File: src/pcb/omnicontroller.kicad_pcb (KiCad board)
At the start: 2 copper layers, 124.5 x 68.6 mm, 52 parts, among them J1 G-Switch GT-USB-7010ASV, J2 USB_A, U1 RP2040, U2 NCP1117ST33T3G, U3 W25Q128JVSIM, X1 SW_Omron_B3FS-1000P, Y1 ABM8-272-T3, Y2 SW_Omron_B3FS-1000P

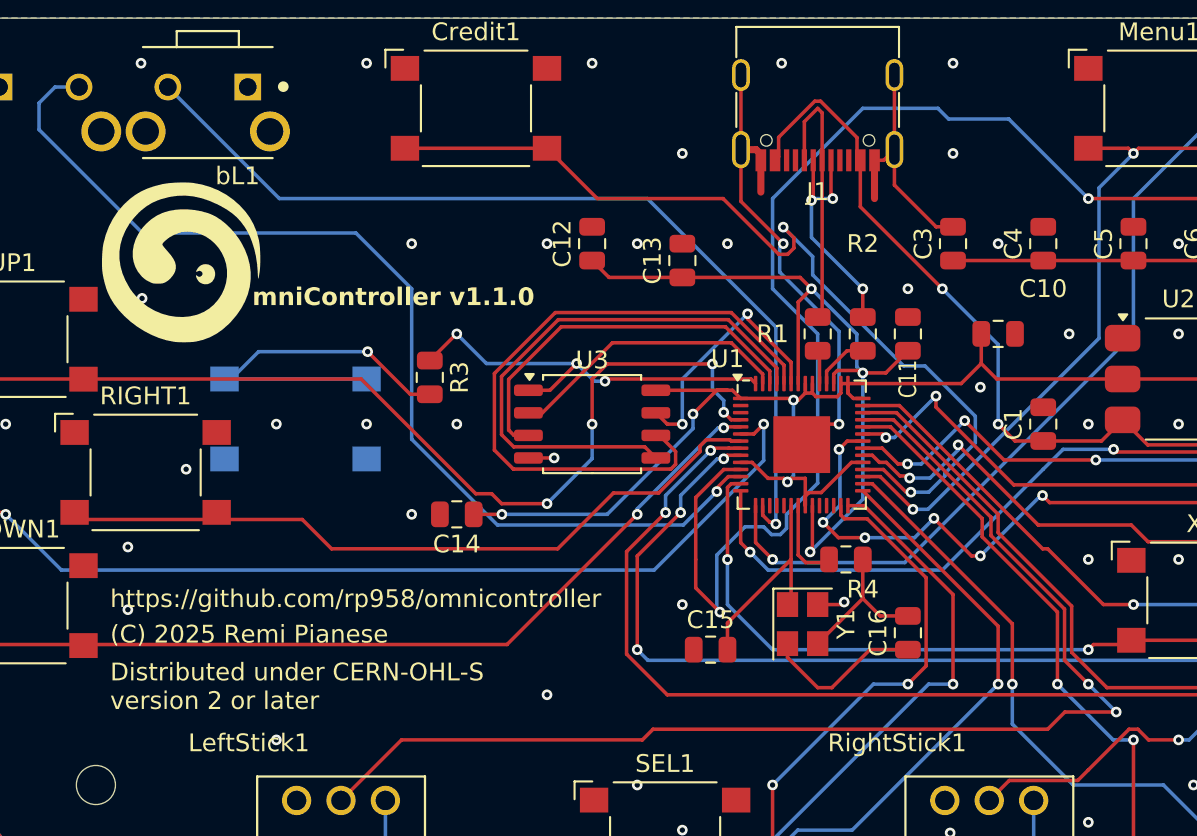
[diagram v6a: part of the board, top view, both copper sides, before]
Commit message: add pinheader with all unused GPIO
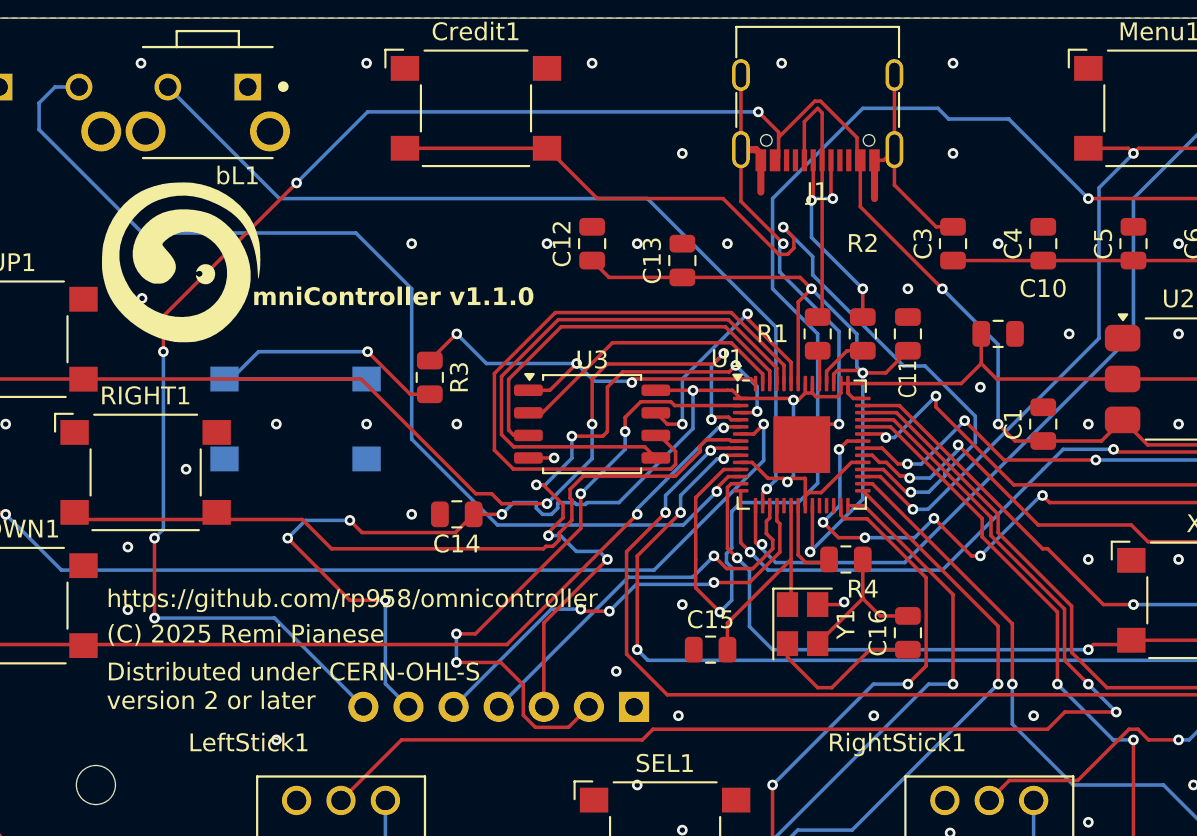
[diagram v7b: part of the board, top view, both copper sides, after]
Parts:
- added J3: Conn_01x07_Pin, Connector_PinHeader_2.54mm:PinHeader_1x07_P2.54mm_Horizontal, B.Cu at (106.5, 84.5)
- START1: value SW_Omron_B3FS-1000P -> SW_Omron_B3FS-1000
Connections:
- U1 pad 17: unconnected-(U1-GPIO14-Pad17) -> GP14
- U1 pad 18: unconnected-(U1-GPIO15-Pad18) -> GP15
- U1 pad 2: unconnected-(U1-GPIO0-Pad2) -> GP00
- U1 pad 3: unconnected-(U1-GPIO1-Pad3) -> GP01
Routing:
- net VBUS: track 83.7 -> 155.0 mm, vias 3 -> 8
- net GP01: track 0.00 -> 38.0 mm, vias 0 -> 6
- net GP00: track 0.00 -> 35.8 mm, vias 0 -> 4
- net +3V3: track 257.1 -> 282.0 mm, vias 7 -> 10
- net GP15: track 0.00 -> 24.8 mm, vias 0 -> 3
- net GP14: track 0.00 -> 22.4 mm, vias 0 -> 1
- net GP02: track 56.3 -> 58.9 mm
- net GP13: track 52.3 -> 50.2 mm
- net GP05: track 41.1 -> 42.5 mm
- net GND: vias 90 -> 93

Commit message: Add 3d models to pcb
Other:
- board text added: "+3.3V"
- board text added: "+5V"
- board text added: "GND"
- board text added: "GP00"
- board text added: "GP01"
- board text added: "GP14"
- board text added: "GP15"
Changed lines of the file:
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@@
 		)
 		(embedded_fonts no)
-		(model "${KICAD6_3DMODEL_DIR}/Button_Switch_SMD.3dshapes/SW_SPST_Omron_B3FS-100xP.wrl"
+		(model "${KIPRJMOD}/libs/Buttons.pretty/B3FS-1000--3DModel-STEP-273799.STEP"
 			(offset
 				(xyz 0 0 0)
@@
 			)
 			(rotate
-				(xyz 0 0 0)
+				(xyz -90 -0 -0)
 			)
 		)
@@
 		)
 		(embedded_fonts no)
-		(model "${KICAD6_3DMODEL_DIR}/Button_Switch_SMD.3dshapes/SW_SPST_Omron_B3FS-100xP.wrl"
+		(model "${KIPRJMOD}/libs/Buttons.pretty/B3FS-1000--3DModel-STEP-273799.STEP"
 			(offset
 				(xyz 0 0 0)
@@
 			)
 			(rotate
-				(xyz 0 0 0)
+				(xyz -90 -0 -0)
 			)
 		)
@@
 		)
 		(embedded_fonts no)
-		(model "${KICAD6_3DMODEL_DIR}/Button_Switch_SMD.3dshapes/SW_SPST_Omron_B3FS-100xP.wrl"
+		(model "${KIPRJMOD}/libs/Buttons.pretty/B3FS-1000--3DModel-STEP-273799.STEP"
 			(offset
 				(xyz 0 0 0)
@@
 			)
 			(rotate
-				(xyz 0 0 0)
+				(xyz -90 -0 -0)
 			)
 		)
@@
 		)
 		(embedded_fonts no)
-		(model "${KICAD6_3DMODEL_DIR}/Button_Switch_SMD.3dshapes/SW_SPST_Omron_B3FS-100xP.wrl"
+		(model "${KIPRJMOD}/libs/Buttons.pretty/B3FS-1000--3DModel-STEP-273799.STEP"
 			(offset
 				(xyz 0 0 0)
@@
 			)
 			(rotate
-				(xyz 0 0 0)
+				(xyz -90 -0 -0)
 			)
 		)
@@
 		)
 		(embedded_fonts no)
-		(model "${KICAD6_3DMODEL_DIR}/Button_Switch_SMD.3dshapes/SW_SPST_Omron_B3FS-100xP.wrl"
+		(model "${KIPRJMOD}/libs/Buttons.pretty/B3FS-1000--3DModel-STEP-273799.STEP"
 			(offset
 				(xyz 0 0 0)
@@
 			)
 			(rotate
-				(xyz 0 0 0)
+				(xyz -90 -0 -0)
 			)
 		)
@@
 		)
 		(embedded_fonts no)
-		(model "${KICAD6_3DMODEL_DIR}/Button_Switch_SMD.3dshapes/SW_SPST_Omron_B3FS-100xP.wrl"
+		(model "${KIPRJMOD}/libs/Buttons.pretty/B3FS-1000--3DModel-STEP-273799.STEP"
 			(offset
 				(xyz 0 0 0)
@@
 			)
 			(rotate
-				(xyz 0 0 0)
+				(xyz -90 -0 -0)
 			)
 		)
@@
 		)
 		(embedded_fonts no)
+		(model "${KIPRJMOD}/libs/Buttons.pretty/B3F-3100--3DModel-STEP-269445.STEP"
+			(offset
+				(xyz 0 -2.2 4)
+			)
+			(scale
+				(xyz 1 1 1)
+			)
+			(rotate
+				(xyz -90 -0 -0)
+			)
+		)
 	)
 	(footprint "Package_SO:SOIC-8_5.3x5.3mm_P1.27mm"
@@
 		)
 		(embedded_fonts no)
-		(model "${KICAD6_3DMODEL_DIR}/Button_Switch_SMD.3dshapes/SW_SPST_Omron_B3FS-100xP.wrl"
+		(model "${KIPRJMOD}/libs/Buttons.pretty/B3FS-1000--3DModel-STEP-273799.STEP"
 			(offset
 				(xyz 0 0 0)
@@
 			)
 			(rotate
-				(xyz 0 0 0)
+				(xyz -90 -0 -0)
 			)
 		)
@@
 		)
 		(embedded_fonts no)
-		(model "${KICAD6_3DMODEL_DIR}/Button_Switch_SMD.3dshapes/SW_SPST_Omron_B3FS-100xP.wrl"
+		(model "${KIPRJMOD}/libs/Buttons.pretty/B3FS-1000--3DModel-STEP-273799.STEP"
 			(offset
 				(xyz 0 0 0)
@@
 			)
 			(rotate
-				(xyz 0 0 0)
+				(xyz -90 -0 -0)
 			)
 		)
@@
 		)
 		(embedded_fonts no)
-		(model "${KICAD6_3DMODEL_DIR}/Button_Switch_SMD.3dshapes/SW_SPST_Omron_B3FS-100xP.wrl"
+		(model "${KIPRJMOD}/libs/Buttons.pretty/B3FS-1000--3DModel-STEP-273799.STEP"
 			(offset
 				(xyz 0 0 0)
@@
 			)
 			(rotate
-				(xyz 0 0 0)
+				(xyz -90 -0 -0)
 			)
 		)
@@
 		)
 		(embedded_fonts no)
-		(model "${KICAD6_3DMODEL_DIR}/Button_Switch_SMD.3dshapes/SW_SPST_Omron_B3FS-100xP.wrl"
+		(model "${KIPRJMOD}/libs/Buttons.pretty/B3FS-1000--3DModel-STEP-273799.STEP"
 			(offset
 				(xyz 0 0 0)
@@
 			)
 			(rotate
-				(xyz 0 0 0)
+				(xyz -90 -0 -0)
 			)
 		)
@@
 		)
 		(embedded_fonts no)
-		(model "${KICAD6_3DMODEL_DIR}/Button_Switch_SMD.3dshapes/SW_SPST_Omron_B3FS-100xP.wrl"
+		(model "${KIPRJMOD}/libs/Buttons.pretty/B3FS-1000--3DModel-STEP-273799.STEP"
 			(offset
 				(xyz 0 0 0)
@@
 			)
 			(rotate
-				(xyz 0 0 0)
+				(xyz -90 -0 -0)
 			)
 		)
@@
 		)
 		(embedded_fonts no)
-		(model "${KICAD6_3DMODEL_DIR}/Button_Switch_SMD.3dshapes/SW_SPST_Omron_B3FS-100xP.wrl"
+		(model "${KIPRJMOD}/libs/Buttons.pretty/B3FS-1000--3DModel-STEP-273799.STEP"
 			(offset
 				(xyz 0 0 0)
@@
 			)
 			(rotate
-				(xyz 0 0 0)
+				(xyz -90 -0 -0)
 			)
 		)
@@
 		)
 		(embedded_fonts no)
+		(model "${KIPRJMOD}/libs/Buttons.pretty/B3F-3100--3DModel-STEP-269445.STEP"
+			(offset
+				(xyz 0 -2.2 4)
+			)
+			(scale
+				(xyz 1 1 1)
+			)
+			(rotate
+				(xyz -90 -0 -0)
+			)
+		)
 	)
 	(footprint "Button_Switch_SMD:SW_SPST_Omron_B3FS-100xP"
@@
 		)
 		(embedded_fonts no)
-		(model "${KICAD6_3DMODEL_DIR}/Button_Switch_SMD.3dshapes/SW_SPST_Omron_B3FS-100xP.wrl"
+		(model "${KIPRJMOD}/libs/Buttons.pretty/B3FS-1000--3DModel-STEP-273799.STEP"
 			(offset
 				(xyz 0 0 0)
@@
 			)
 			(rotate
-				(xyz 0 0 0)
+				(xyz -90 -0 -0)
 			)
 		)
@@
 		)
 		(embedded_fonts no)
-		(model "${KICAD6_3DMODEL_DIR}/Button_Switch_SMD.3dshapes/SW_SPST_Omron_B3FS-100xP.wrl"
+		(model "${KIPRJMOD}/libs/Buttons.pretty/B3FS-1000--3DModel-STEP-273799.STEP"
 			(offset
 				(xyz 0 0 0)
@@
 			)
 			(rotate
-				(xyz 0 0 0)
+				(xyz -90 -0 -0)
 			)
 		)
@@
 		)
 		(embedded_fonts no)
-		(model "${KICAD6_3DMODEL_DIR}/Button_Switch_SMD.3dshapes/SW_SPST_Omron_B3FS-100xP.wrl"
+		(model "${KIPRJMOD}/libs/Buttons.pretty/B3FS-1000--3DModel-STEP-273799.STEP"
 			(offset
 				(xyz 0 0 0)
@@
 			)
 			(rotate
-				(xyz 0 0 0)
+				(xyz -90 -0 -0)
 			)
 		)
@@
 		)
 		(embedded_fonts no)
+		(model "${KIPRJMOD}/libs/Buttons.pretty/B3F-3100--3DModel-STEP-269445.STEP"
+			(offset
+				(xyz 0 -2.2 4)
+			)
+			(scale
+				(xyz 1 1 1)
+			)
+			(rotate
+				(xyz -90 -0 -0)
+			)
+		)
 	)
 	(footprint "Buttons:SW_B3F-3100"
@@
 		)
 		(embedded_fonts no)
+		(model "${KIPRJMOD}/libs/Buttons.pretty/B3F-3100--3DModel-STEP-269445.STEP"
+			(offset
+				(xyz 0 -2.2 4)
+			)
+			(scale
+				(xyz 1 1 1)
+			)
+			(rotate
+				(xyz -90 -0 -0)
+			)
+		)
 	)
 	(footprint "Connector_USB:USB_A_Receptacle_GCT_USB1046"
@@
 		)
 		(embedded_fonts no)
-		(model "${KICAD9_3DMODEL_DIR}/Connector_USB.3dshapes/USB_A_Receptacle_GCT_USB1046.wrl"
+		(model "${KICAD9_3DMODEL_DIR}/Connector_USB.3dshapes/USB_A_TE_292303-7_Horizontal.step"
 			(offset
-				(xyz 0 0 0)
+				(xyz 0 0.6 0)
 			)
 			(scale
@@
 			)
 			(rotate
-				(xyz 0 0 0)
+				(xyz -0 -0 -0)
 			)
 		)
@@
 		)
 	)
+	(gr_text "GP14"
+		(at 100 87 0)
+		(layer "B.SilkS")
+		(effects
+			(font
+				(size 0.8 0.5)
+				(thickness 0.1)
+			)
+			(justify left bottom mirror)
+		)
+	)
+	(gr_text "+3.3V"
+		(at 95 87 0)
+		(layer "B.SilkS")
+		(effects
+			(font
+				(size 0.8 0.5)
+				(thickness 0.1)
+			)
+			(justify left bottom mirror)
+		)
+	)
+	(gr_text "+5V"
+		(at 92 87 0)
+		(layer "B.SilkS")
+		(effects
+			(font
+				(size 0.8 0.5)
+				(thickness 0.1)
+			)
+			(justify left bottom mirror)
+		)
+	)
+	(gr_text "GND"
+		(at 107.3 87 0)
+		(layer "B.SilkS")
+		(effects
+			(font
+				(size 0.8 0.5)
+				(thickness 0.1)
+			)
+			(justify left bottom mirror)
+		)
+	)
+	(gr_text "GP00"
+		(at 105 87 0)
+		(layer "B.SilkS")
+		(effects
+			(font
+				(size 0.8 0.5)
+				(thickness 0.1)
+			)
+			(justify left bottom mirror)
+		)
+	)
+	(gr_text "GP15"
+		(at 97.5 87 0)
+		(layer "B.SilkS")
+		(effects
+			(font
+				(size 0.8 0.5)
+				(thickness 0.1)
+			)
+			(justify left bottom mirror)
+		)
+	)
+	(gr_text "GP01"
+		(at 102.5 87 0)
+		(layer "B.SilkS")
+		(effects
+			(font
+				(size 0.8 0.5)
+				(thickness 0.1)
+			)
+			(justify left bottom mirror)
+		)
+	)
